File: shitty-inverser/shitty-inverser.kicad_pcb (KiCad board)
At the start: 2 copper layers, 10 x 15 mm, 2 parts, among them J1 SAO, J2 Badge

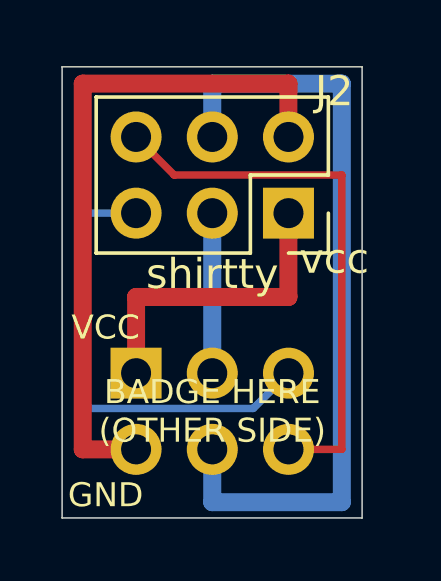
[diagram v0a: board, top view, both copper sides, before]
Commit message: feature: route inverser so it works without metallized hole
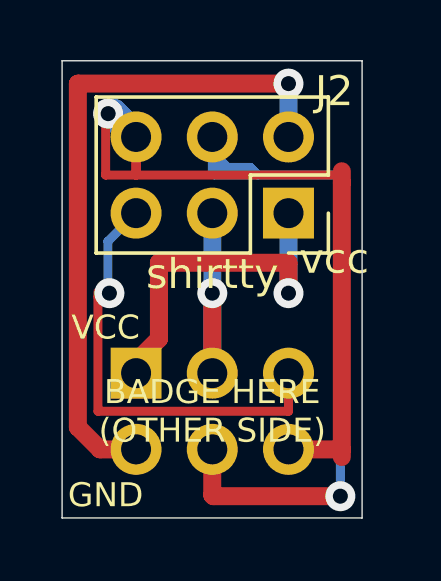
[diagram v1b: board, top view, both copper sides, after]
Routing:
- net /GPIO2: track 18.3 -> 26.0 mm, vias 0 -> 1
- net /SDA: track 5.33 -> 7.87 mm, vias 0 -> 1
- net /VCC: track 10.4 -> 12.0 mm, vias 0 -> 1
- net /GPIO1: track 15.6 -> 14.3 mm, vias 0 -> 1
- net /SCL: track 26.1 -> 25.7 mm, vias 0 -> 1
- net /GND: track 22.6 -> 22.5 mm, vias 0 -> 1
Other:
- board size 10 x 15 mm -> 10 x 15.2 mm
- net class Default: trace_width 0.25 -> 0.3; via_dia 0.8 -> 1; via_drill 0.4 -> 0.5
- rule trace_min: 0.2 -> 0.3
- board text added: "Connector for badge is on top side. All solder joints are be on bottom (green)"
- board text added: "Connector to badge is on bottom side. All solder joints are on top (red)."
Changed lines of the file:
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@@
   (general
     (thickness 1.6)
-    (drawings 9)
-    (tracks 22)
+    (drawings 11)
+    (tracks 58)
     (zones 0)
     (modules 2)
@@
   )
   (setup
-    (last_trace_width 0.25)
+    (last_trace_width 1)
     (user_trace_width 0.6)
     (user_trace_width 1)
@@
     (zone_clearance 0.508)
     (zone_45_only no)
-    (trace_min 0.2)
-    (via_size 0.8)
-    (via_drill 0.4)
+    (trace_min 0.3)
+    (via_size 1)
+    (via_drill 0.5)
     (via_min_size 0.4)
     (via_min_drill 0.3)
@@
   (net_class Default "This is the default net class."
     (clearance 0.2)
-    (trace_width 0.25)
-    (via_dia 0.8)
-    (via_drill 0.4)
+    (trace_width 0.3)
+    (via_dia 1)
+    (via_drill 0.5)
     (uvia_dia 0.3)
     (uvia_drill 0.1)
+    (diff_pair_width 0.5)
+    (diff_pair_gap 0.25)
     (add_net /GND)
     (add_net /GPIO1)
@@
     )
   )
+  (gr_text "Connector for badge is on top side.\nAll solder joints are be on bottom (green)" (at 92.456 55.372) (layer F.Fab)
+    (effects (font (size 0.5 0.5) (thickness 0.1)) (justify left))
+  )
+  (gr_text "Connector to badge is on bottom side.\nAll solder joints are on top (red)." (at 92.456 63.246) (layer F.Fab)
+    (effects (font (size 0.5 0.5) (thickness 0.1)) (justify left))
+  )
   (gr_text vcc (at 90.424 58.42) (layer F.SilkS)
     (effects (font (size 1 1) (thickness 0.15)))
@@
     (effects (font (size 0.8 0.8) (thickness 0.1)))
   )
-  (gr_line (start 81.354 52.018) (end 81.354 67.056) (layer Edge.Cuts) (width 0.05))
-  (gr_line (start 91.354 52.018) (end 81.354 52.018) (layer Edge.Cuts) (width 0.05))
-  (gr_line (start 91.354 67.056) (end 91.354 52.018) (layer Edge.Cuts) (width 0.05))
+  (gr_line (start 81.354 51.816) (end 81.354 67.056) (layer Edge.Cuts) (width 0.05))
+  (gr_line (start 91.354 51.816) (end 81.354 51.816) (layer Edge.Cuts) (width 0.05))
+  (gr_line (start 91.354 67.056) (end 91.354 51.816) (layer Edge.Cuts) (width 0.05))
   (gr_line (start 81.354 67.056) (end 91.354 67.056) (layer Edge.Cuts) (width 0.05))
-  (segment (start 85.09 55.626) (end 83.82 54.356) (width 0.25) (layer F.Cu) (net 1))
-  (segment (start 90.678 55.626) (end 85.09 55.626) (width 0.25) (layer F.Cu) (net 1))
-  (segment (start 90.678 64.77) (end 90.678 55.626) (width 0.25) (layer F.Cu) (net 1))
-  (segment (start 88.9 64.77) (end 90.678 64.77) (width 0.25) (layer F.Cu) (net 1))
-  (segment (start 82.042 56.896) (end 83.82 56.896) (width 0.25) (layer B.Cu) (net 2))
-  (segment (start 82.042 63.310002) (end 82.042 56.896) (width 0.25) (layer B.Cu) (net 2))
-  (segment (start 82.136999 63.405001) (end 82.042 63.310002) (width 0.25) (layer B.Cu) (net 2))
-  (segment (start 87.724999 63.405001) (end 82.136999 63.405001) (width 0.25) (layer B.Cu) (net 2))
-  (segment (start 88.9 62.23) (end 87.724999 63.405001) (width 0.25) (layer B.Cu) (net 2))
-  (segment (start 86.36 52.578) (end 86.36 54.356) (width 0.6) (layer B.Cu) (net 3))
-  (segment (start 86.36 66.53099) (end 90.678 66.53099) (width 0.6) (layer B.Cu) (net 3))
-  (segment (start 90.678 52.578) (end 86.36 52.578) (width 0.6) (layer B.Cu) (net 3))
-  (segment (start 90.678 66.53099) (end 90.678 52.578) (width 0.6) (layer B.Cu) (net 3))
-  (segment (start 86.36 64.77) (end 86.36 66.53099) (width 0.6) (layer B.Cu) (net 3))
-  (segment (start 86.36 62.23) (end 86.36 56.896) (width 0.6) (layer B.Cu) (net 4))
-  (segment (start 88.9 52.578) (end 88.9 54.356) (width 0.6) (layer F.Cu) (net 5))
-  (segment (start 82.042 52.578) (end 88.9 52.578) (width 0.6) (layer F.Cu) (net 5))
-  (segment (start 82.042 64.77) (end 82.042 52.578) (width 0.6) (layer F.Cu) (net 5))
-  (segment (start 83.82 64.77) (end 82.042 64.77) (width 0.6) (layer F.Cu) (net 5))
-  (segment (start 88.9 59.69) (end 88.9 56.896) (width 0.6) (layer F.Cu) (net 6))
-  (segment (start 83.82 59.69) (end 88.9 59.69) (width 0.6) (layer F.Cu) (net 6))
-  (segment (start 83.82 62.23) (end 83.82 59.69) (width 0.6) (layer F.Cu) (net 6))
+  (segment (start 88.9 64.77) (end 90.678 64.77) (width 0.6) (layer F.Cu) (net 1))
+  (segment (start 90.678 65.024) (end 90.678 55.88) (width 0.6) (layer F.Cu) (net 1))
+  (segment (start 83.82 55.626) (end 83.82 54.356) (width 0.3) (layer F.Cu) (net 1))
+  (via (at 82.889022 53.57801) (size 1) (drill 0.5) (layers F.Cu B.Cu) (net 1))
+  (segment (start 83.82 54.508988) (end 83.389021 54.078009) (width 0.3) (layer F.Cu) (net 1))
+  (segment (start 83.389021 54.078009) (end 82.889022 53.57801) (width 0.3) (layer F.Cu) (net 1))
+  (segment (start 83.82 55.626) (end 83.82 54.508988) (width 0.3) (layer F.Cu) (net 1))
+  (segment (start 82.804 55.626) (end 82.804 53.663032) (width 0.3) (layer F.Cu) (net 1))
+  (segment (start 82.804 53.663032) (end 82.889022 53.57801) (width 0.3) (layer F.Cu) (net 1))
+  (segment (start 83.82 55.626) (end 82.804 55.626) (width 0.3) (layer F.Cu) (net 1))
+  (segment (start 83.82 55.626) (end 90.424 55.626) (width 0.3) (layer F.Cu) (net 1))
+  (segment (start 90.678 55.88) (end 90.678 55.499) (width 0.6) (layer F.Cu) (net 1))
+  (segment (start 83.04201 53.57801) (end 83.82 54.356) (width 1) (layer B.Cu) (net 1))
+  (segment (start 82.889022 53.57801) (end 83.04201 53.57801) (width 1) (layer B.Cu) (net 1))
+  (segment (start 88.9 62.23) (end 88.9 63.5) (width 0.3) (layer F.Cu) (net 2))
+  (segment (start 88.9 63.5) (end 82.55 63.5) (width 0.3) (layer F.Cu) (net 2))
+  (segment (start 82.55 63.5) (end 82.55 59.69) (width 0.3) (layer F.Cu) (net 2))
+  (via (at 82.931 59.563) (size 1) (drill 0.5) (layers F.Cu B.Cu) (net 2))
+  (segment (start 82.55 59.69) (end 82.55 59.511024) (width 0.3) (layer F.Cu) (net 2))
+  (segment (start 82.879024 57.836976) (end 83.82 56.896) (width 0.3) (layer B.Cu) (net 2))
+  (segment (start 82.879024 59.182) (end 82.879024 57.836976) (width 0.3) (layer B.Cu) (net 2))
+  (segment (start 90.678 66.38) (end 90.629 66.331) (width 0.6) (layer B.Cu) (net 3))
+  (via (at 90.629 66.331) (size 1) (drill 0.5) (layers F.Cu B.Cu) (net 3))
+  (segment (start 90.629 66.331) (end 86.397 66.331) (width 0.6) (layer F.Cu) (net 3))
+  (segment (start 86.36 66.294) (end 86.36 64.77) (width 0.6) (layer F.Cu) (net 3))
+  (segment (start 86.397 66.331) (end 86.36 66.294) (width 0.6) (layer F.Cu) (net 3))
+  (segment (start 86.427919 55.626) (end 86.36 55.558081) (width 0.3) (layer B.Cu) (net 3))
+  (segment (start 86.36 55.558081) (end 86.36 54.356) (width 0.3) (layer B.Cu) (net 3))
+  (segment (start 90.629 66.331) (end 90.629 55.671999) (width 0.3) (layer B.Cu) (net 3))
+  (segment (start 86.36 55.118) (end 86.614 55.372) (width 0.3) (layer B.Cu) (net 3))
+  (segment (start 90.583001 55.626) (end 87.884 55.626) (width 0.3) (layer B.Cu) (net 3))
+  (segment (start 86.36 54.356) (end 86.36 55.118) (width 0.3) (layer B.Cu) (net 3))
+  (segment (start 87.63 55.372) (end 87.884 55.626) (width 0.3) (layer B.Cu) (net 3))
+  (segment (start 87.884 55.626) (end 86.427919 55.626) (width 0.3) (layer B.Cu) (net 3))
+  (segment (start 86.36 54.864) (end 86.868 55.372) (width 0.3) (layer B.Cu) (net 3))
+  (segment (start 86.36 54.356) (end 86.36 54.864) (width 0.3) (layer B.Cu) (net 3))
+  (segment (start 86.868 55.372) (end 87.63 55.372) (width 0.3) (layer B.Cu) (net 3))
+  (segment (start 86.614 55.372) (end 86.868 55.372) (width 0.3) (layer B.Cu) (net 3))
+  (segment (start 86.36 58.42) (end 86.36 56.896) (width 0.6) (layer B.Cu) (net 4))
+  (via (at 86.36 59.563) (size 1) (drill 0.5) (layers F.Cu B.Cu) (net 4))
+  (segment (start 86.36 62.23) (end 86.36 59.69) (width 0.6) (layer F.Cu) (net 4))
+  (segment (start 86.36 59.69) (end 86.36 62.23) (width 0.6) (layer B.Cu) (net 4))
+  (segment (start 86.36 58.42) (end 86.36 59.69) (width 0.6) (layer B.Cu) (net 4))
+  (via (at 88.9 52.578) (size 1) (drill 0.5) (layers F.Cu B.Cu) (net 5))
+  (segment (start 88.9 52.832) (end 88.9 54.356) (width 0.6) (layer B.Cu) (net 5))
+  (segment (start 88.711 52.643) (end 88.9 52.832) (width 0.6) (layer B.Cu) (net 5))
+  (segment (start 81.87901 64.031091) (end 82.617919 64.77) (width 0.6) (layer F.Cu) (net 5))
+  (segment (start 88.9 52.578) (end 81.889012 52.578) (width 0.6) (layer F.Cu) (net 5))
+  (segment (start 81.889012 52.578) (end 81.87901 52.588002) (width 0.6) (layer F.Cu) (net 5))
+  (segment (start 81.87901 52.588002) (end 81.87901 64.031091) (width 0.6) (layer F.Cu) (net 5))
+  (segment (start 82.617919 64.77) (end 83.82 64.77) (width 0.6) (layer F.Cu) (net 5))
+  (segment (start 83.82 62.23) (end 83.82 61.849) (width 0.6) (layer F.Cu) (net 6))
+  (segment (start 83.82 61.849) (end 84.582 61.087) (width 0.6) (layer F.Cu) (net 6))
+  (segment (start 84.582 61.087) (end 84.582 58.547) (width 0.6) (layer F.Cu) (net 6))
+  (segment (start 84.582 58.547) (end 88.9 58.547) (width 0.6) (layer F.Cu) (net 6))
+  (via (at 88.9 59.563) (size 1) (drill 0.5) (layers F.Cu B.Cu) (net 6))
+  (segment (start 88.9 58.547) (end 88.9 59.563) (width 0.6) (layer F.Cu) (net 6))
+  (segment (start 88.9 59.563) (end 88.9 56.896) (width 0.6) (layer B.Cu) (net 6))
 )
